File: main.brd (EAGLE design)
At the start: 50.8 x 50.8 mm, 104 parts, among them Q1 5.8A/30V/35mΩ, Q2 5.8A/30V/35mΩ, Q3 2.5A/30V/105mΩ, U2 SN65HVD32_D_8

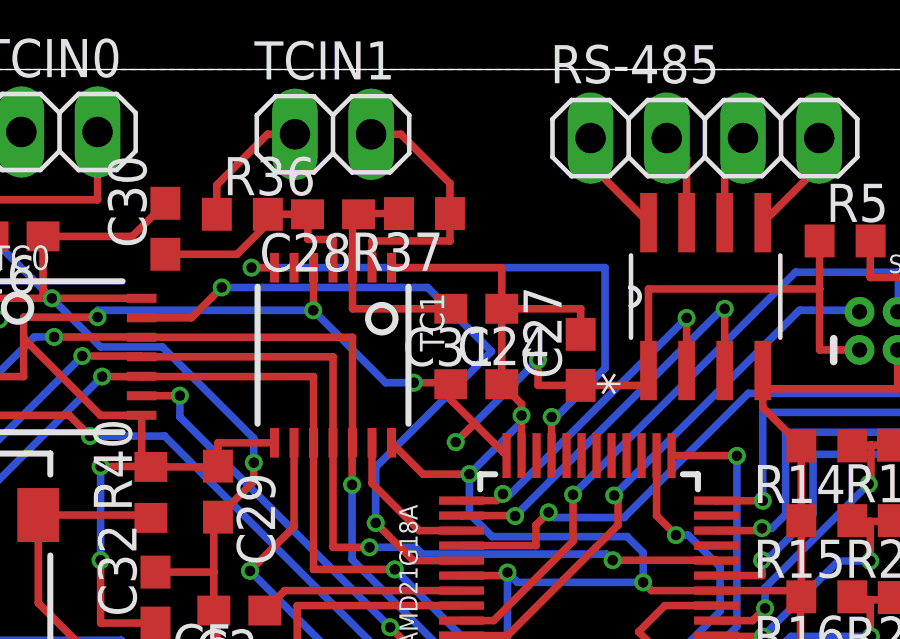
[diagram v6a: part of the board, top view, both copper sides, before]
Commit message: Updated 3.3reg values, fixed led resitor, added one led to mcu
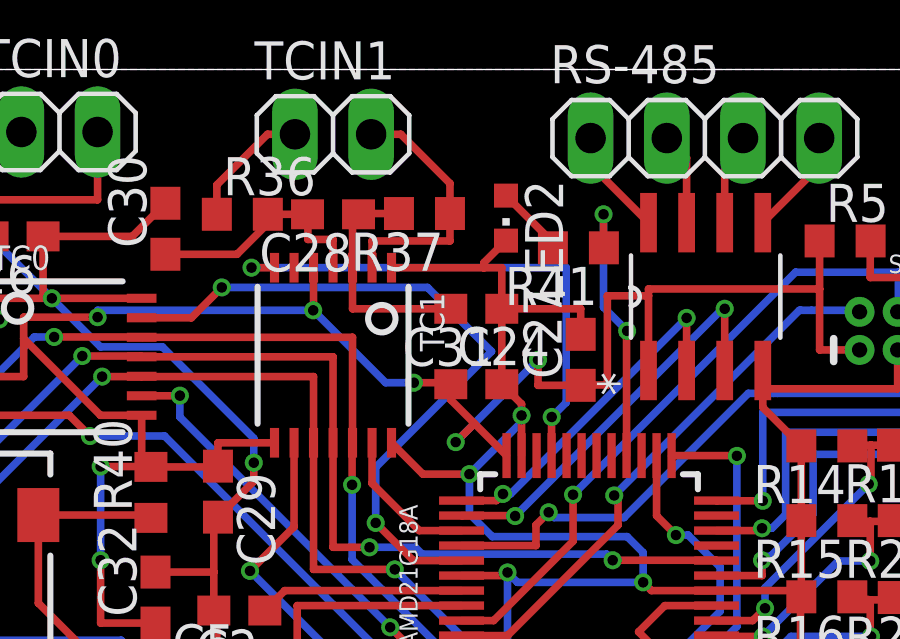
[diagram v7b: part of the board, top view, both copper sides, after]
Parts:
- added LED2: 2V @ 20mA, adafruit:CHIPLED_0603
- added R41: 65, resistor:R0603
- C6: value REF -> 22u
- C7: value REF -> 10u
- L1: value REF -> 2.2u
- LED1: value (none) -> 2V @ 20mA
- R1: value REF -> 470k
- R2: value REF -> 150k
- R3: value REF -> 100k
- R32: value 1.5k -> 65
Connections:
- new net LED: R41.1, SAMD21G18A.28
- new net N$29: LED2.A, R41.2
- net GND: now also LED2.C
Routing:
- net LED: track 0.00 -> 9.50 mm, vias 0 -> 2
- net 3.3V: track 181.5 -> 184.5 mm
- net N$29: track 0.00 -> 2.39 mm
- net TC1_DRDY: track 19.6 -> 17.7 mm
- net GND: track 345.4 -> 346.6 mm

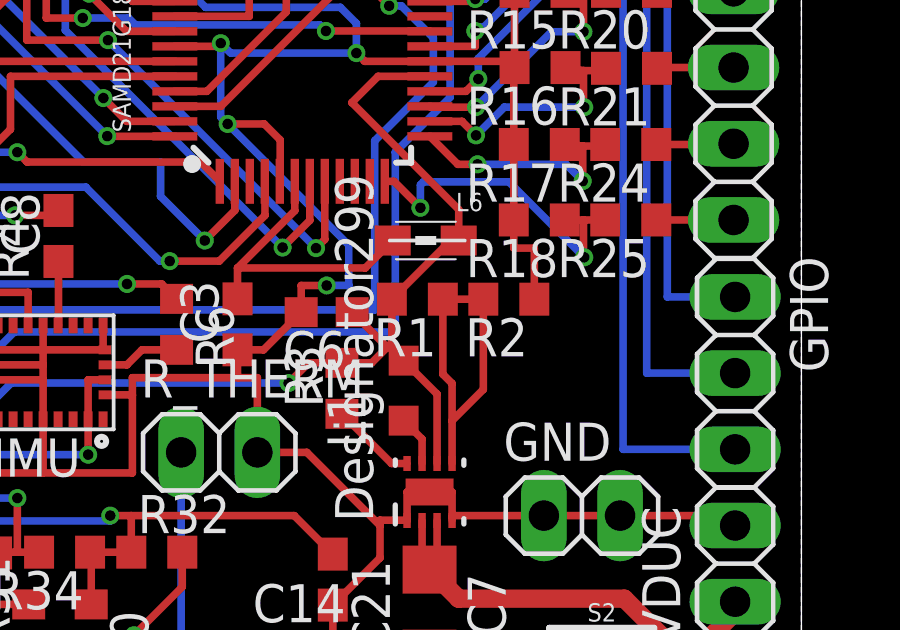
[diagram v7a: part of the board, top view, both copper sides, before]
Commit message: Fixed 3.3v reg
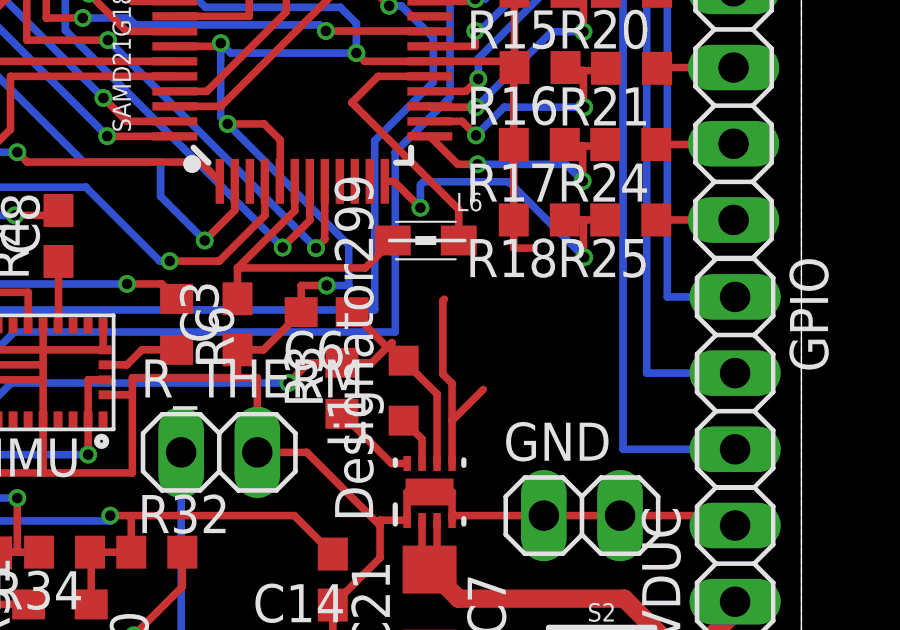
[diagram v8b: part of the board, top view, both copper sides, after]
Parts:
- removed R1: 470k, resistor:R0603
- removed R2: 150k, resistor:R0603
- renumbered 3.3V_REG to TPS62162-Q1
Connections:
- removed net N$10: R1.1, R2.2, TPS62162-Q1.5
- net 3.3V: no longer R1.2
- net GND: now also TPS62162-Q1.5; no longer R2.1
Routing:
- net N$10: track 11.5 -> 0.00 mm
- net GND: track 346.6 -> 352.0 mm
- net 3.3V: track 184.5 -> 180.2 mm
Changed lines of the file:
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@@
 <?xml version="1.0" encoding="utf-8"?>
 <!DOCTYPE eagle SYSTEM "eagle.dtd">
-<eagle version="8.5.2">
+<eagle version="8.5.1">
 <drawing>
 <settings>
@@
 <attribute name="PRICE" value="7.78 USD" x="25.273" y="23.0632" size="1.778" layer="27" rot="R180" display="off"/>
 </element>
-<element name="3.3V_REG" library="TPS62162-Q1" package="DSG0008A" value="" x="38.4048" y="19.0754" rot="R90">
+<element name="TPS62162-Q1" library="TPS62162-Q1" package="DSG0008A" value="" x="38.4048" y="19.0754" rot="R90">
 <attribute name="MANUFACTURER" value="Texas Instruments" x="38.4048" y="19.0754" size="1.778" layer="27" rot="R90" display="off"/>
 <attribute name="PARTNUMBER" value="TPS62162QDSGRQ1" x="38.4048" y="19.0754" size="1.778" layer="27" rot="R90" display="off"/>
@@
 <attribute name="TYPE" value="TYPE" x="38.4048" y="19.0754" size="1.778" layer="27" rot="R90" display="off"/>
 </element>
-<element name="R1" library="resistor" library_urn="urn:adsk.eagle:library:348" package="R0603" package3d_urn="urn:adsk.eagle:package:26057/1" value="470k" x="37.9984" y="25.5016" rot="R180"/>
-<element name="R2" library="resistor" library_urn="urn:adsk.eagle:library:348" package="R0603" package3d_urn="urn:adsk.eagle:package:26057/1" value="150k" x="41.0464" y="25.5016" rot="R180"/>
 <element name="R3" library="resistor" library_urn="urn:adsk.eagle:library:348" package="R0603" package3d_urn="urn:adsk.eagle:package:26057/1" value="100k" x="35.4838" y="22.5298" rot="R90"/>
 <element name="L1" library="resistor" library_urn="urn:adsk.eagle:library:348" package="L2012C" package3d_urn="urn:adsk.eagle:package:25925/1" value="2.2u" x="37.5412" y="22.4536" rot="R90"/>
@@
 <contactref element="SWD" pad="1"/>
 <contactref element="SER4" pad="VCC"/>
-<contactref element="3.3V_REG" pad="6"/>
-<contactref element="R1" pad="2"/>
+<contactref element="TPS62162-Q1" pad="6"/>
 <contactref element="R3" pad="2"/>
 <contactref element="L1" pad="2"/>
@@
 <wire x1="38.6548" y1="20.0254" x2="38.6548" y2="22.34" width="0.254" layer="1"/>
 <wire x1="38.6548" y1="22.34" x2="37.5412" y2="23.4536" width="0.254" layer="1"/>
-<wire x1="37.1484" y1="25.5016" x2="37.1484" y2="24.0538" width="0.254" layer="1"/>
 <wire x1="37.1484" y1="24.0538" x2="37.1484" y2="23.8464" width="0.254" layer="1"/>
 <wire x1="37.1484" y1="23.8464" x2="37.5412" y2="23.4536" width="0.254" layer="1"/>
@@
 <via x="17.1704" y="22.9616" extent="1-16" drill="0.35"/>
 <wire x1="39.3778" y1="27.4574" x2="39.1042" y2="27.4574" width="0.254" layer="1"/>
-<wire x1="39.1042" y1="27.4574" x2="37.1484" y2="25.5016" width="0.254" layer="1"/>
 <wire x1="39.3778" y1="27.4574" x2="39.3778" y2="28.491" width="0.254" layer="1"/>
 <wire x1="39.3778" y1="28.491" x2="35.814" y2="32.0548" width="0.254" layer="1"/>
@@
 <wire x1="34.7726" y1="40.2844" x2="33.8836" y2="40.2844" width="0.254" layer="1"/>
 <wire x1="33.8836" y1="40.2844" x2="33.8836" y2="40.2726" width="0.254" layer="1"/>
+<wire x1="37.1484" y1="24.0538" x2="39.1042" y2="27.4574" width="0" layer="19" extent="1-1"/>
 </signal>
 <signal name="GND">
@@
 <contactref element="SER4" pad="GND3"/>
 <contactref element="SER4" pad="GND1"/>
-<contactref element="3.3V_REG" pad="1"/>
-<contactref element="3.3V_REG" pad="4"/>
-<contactref element="3.3V_REG" pad="9"/>
+<contactref element="TPS62162-Q1" pad="1"/>
+<contactref element="TPS62162-Q1" pad="4"/>
+<contactref element="TPS62162-Q1" pad="9"/>
 <contactref element="C7" pad="2"/>
-<contactref element="R2" pad="1"/>
 <contactref element="C6" pad="2"/>
 <contactref element="IMU" pad="25"/>
@@
 <wire x1="41.0092" y1="33.147" x2="41.2378" y2="33.2232" width="0.254" layer="1"/>
 <wire x1="41.2124" y1="30.6578" x2="40.9838" y2="30.6324" width="0.254" layer="1"/>
-<wire x1="41.8964" y1="25.5016" x2="41.8964" y2="27.2052" width="0.254" layer="1"/>
 <contactref element="SER4" pad="CD2"/>
 <wire x1="27.5855" y1="22.3132" x2="28.4868" y2="22.3132" width="0.254" layer="1"/>
@@
 <wire x1="31.3944" y1="45.097" x2="30.6578" y2="44.3604" width="0.254" layer="1"/>
 <wire x1="30.6578" y1="44.3604" x2="30.6578" y2="44.1928" width="0.254" layer="1"/>
+<contactref element="TPS62162-Q1" pad="5"/>
+<wire x1="39.1548" y1="20.0254" x2="39.1548" y2="21.451" width="0.254" layer="1"/>
+<wire x1="39.1548" y1="21.451" x2="40.1964" y2="22.4926" width="0.254" layer="1"/>
+<wire x1="39.1548" y1="21.451" x2="39.1548" y2="22.6942" width="0.254" layer="1"/>
+<wire x1="38.8484" y1="23.0006" x2="38.8484" y2="25.4508" width="0.254" layer="1"/>
+<wire x1="39.1548" y1="22.6942" x2="38.8484" y2="23.0006" width="0.254" layer="1"/>
+<wire x1="38.8992" y1="25.5016" x2="38.8484" y2="25.4508" width="0.254" layer="1"/>
+<wire x1="39.1548" y1="19.0754" x2="39.1548" y2="20.0254" width="0" layer="19" extent="1-1"/>
 </signal>
 <signal name="VDDCORE">
@@
 </signal>
 <signal name="PG">
-<contactref element="3.3V_REG" pad="8"/>
+<contactref element="TPS62162-Q1" pad="8"/>
 <contactref element="R3" pad="1"/>
 <wire x1="37.6548" y1="20.0254" x2="37.1382" y2="20.0254" width="0.254" layer="1"/>
@@
 </signal>
 <signal name="N$7">
-<contactref element="3.3V_REG" pad="7"/>
+<contactref element="TPS62162-Q1" pad="7"/>
 <contactref element="L1" pad="1"/>
 <wire x1="37.5412" y1="21.4536" x2="38.154796875" y2="20.840003125" width="0.254" layer="1"/>
 <wire x1="38.154796875" y1="20.840003125" x2="38.154796875" y2="20.0254" width="0.254" layer="1"/>
-</signal>
-<signal name="N$10">
-<contactref element="R2" pad="2"/>
-<contactref element="R1" pad="1"/>
-<contactref element="3.3V_REG" pad="5"/>
-<wire x1="39.1548" y1="20.0254" x2="39.1548" y2="21.451" width="0.254" layer="1"/>
-<wire x1="40.1964" y1="22.4926" x2="40.1964" y2="25.5016" width="0.254" layer="1"/>
-<wire x1="39.1548" y1="21.451" x2="40.1964" y2="22.4926" width="0.254" layer="1"/>
-<wire x1="39.1548" y1="21.451" x2="39.1548" y2="22.6942" width="0.254" layer="1"/>
-<wire x1="38.8484" y1="23.0006" x2="38.8484" y2="25.4508" width="0.254" layer="1"/>
-<wire x1="38.8484" y1="25.4508" x2="38.8484" y2="25.5016" width="0.254" layer="1"/>
-<wire x1="39.1548" y1="22.6942" x2="38.8484" y2="23.0006" width="0.254" layer="1"/>
-<wire x1="40.1964" y1="25.5016" x2="38.8992" y2="25.5016" width="0.254" layer="1"/>
-<wire x1="38.8992" y1="25.5016" x2="38.8484" y2="25.4508" width="0.254" layer="1"/>
 </signal>
 <signal name="N$9">
@@
 </signal>
 <signal name="VSYS">
-<contactref element="3.3V_REG" pad="2"/>
-<contactref element="3.3V_REG" pad="3"/>
+<contactref element="TPS62162-Q1" pad="2"/>
+<contactref element="TPS62162-Q1" pad="3"/>
 <contactref element="C7" pad="1"/>
 <contactref element="VDUC" pad="1"/>
